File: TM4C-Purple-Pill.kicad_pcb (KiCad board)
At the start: 2 copper layers, 20.3 x 55.9 mm, 31 parts, among them IC1 TM4C123GH6PMI7R, J1 Conn_01x22, J2 Conn_01x22, J3 Conn_02x05_Odd_Even, J5 USB_B_Micro, U1 TLV75533PDBV, Y1 ABM3-16.000MHZ-B2-T, Y2 AB26TRB-32.768KHZ-T

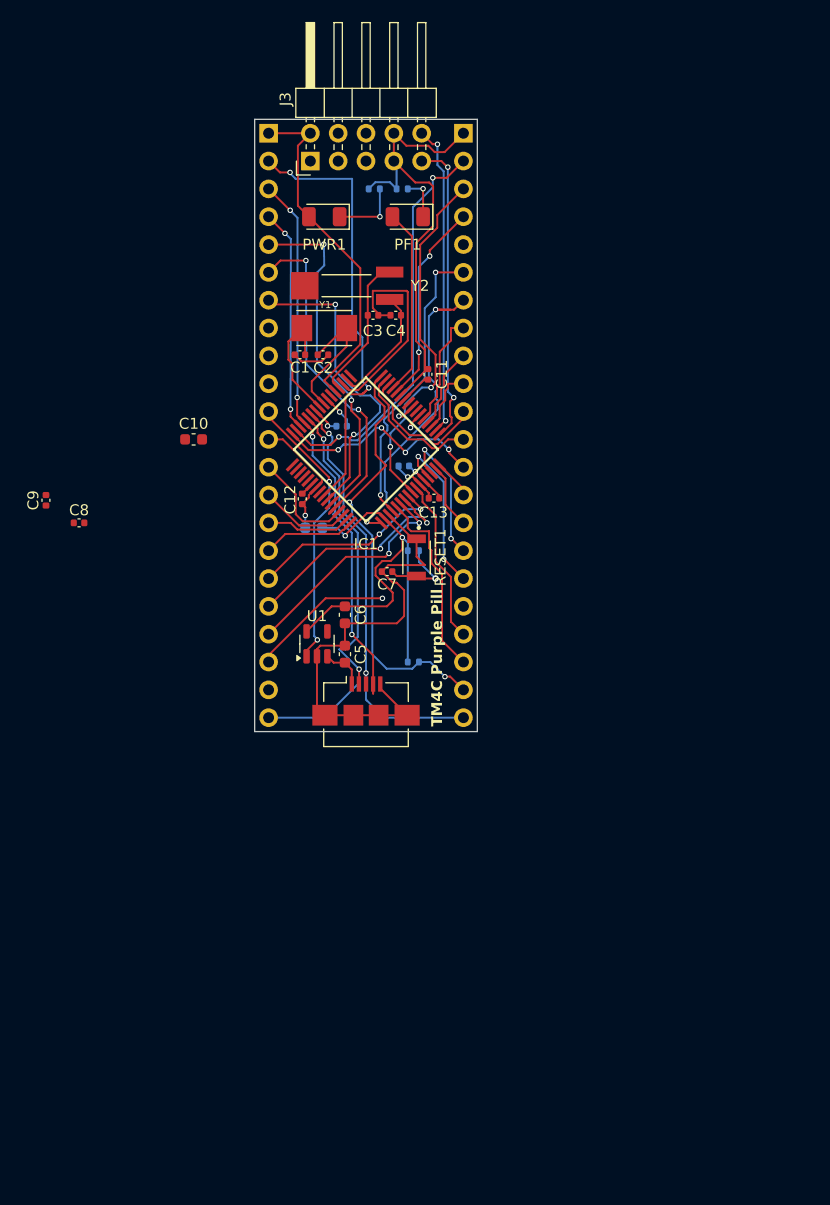
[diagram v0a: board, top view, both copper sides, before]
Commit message: Rehauled GPIO pinout. Need to find NRST wiring
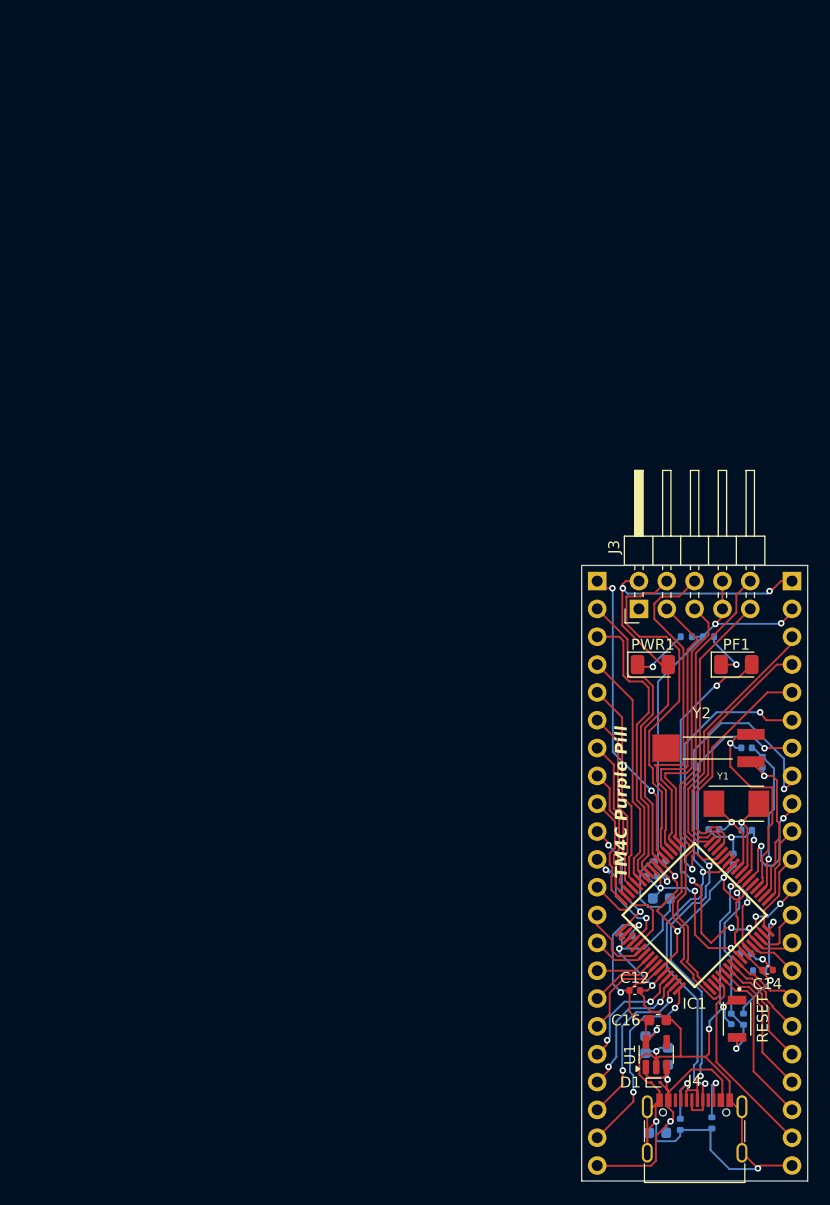
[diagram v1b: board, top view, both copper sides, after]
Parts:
- removed J5: USB_B_Micro, Connector_USB:USB_Micro-B_Amphenol_10104110_Horizontal
- removed RESET1: B3U-1000P, B3U-1000P:SW_B3U-1000P
- added 5.1k1: R5, Resistor_SMD:R_0402_1005Metric, B.Cu at (142.1, 141.1)
- added C17: 1uF, Capacitor_SMD:C_0603_1608Metric, B.Cu at (137.1, 142.0)
- added D1: ESD9B3.3ST5G, Diode_SMD:D_SOD-923, F.Cu at (136.9, 137.4)
- added J4: USB_C_Receptacle_USB2.0_16P, Connector_USB:USB_C_Receptacle_G-Switch_GT-USB-7010ASV, F.Cu at (140.5, 142.8)
- added R4: 5.1k, Resistor_SMD:R_0402_1005Metric, B.Cu at (139.2, 141.3)
- added RESET: B3U-1000P, B3U-1000P:SW_B3U-1000P, F.Cu at (144.4, 131.6)
- C1, C10, C11, C13, C2, C3, C4, C5, C6, C7, C8, C9: moved to B.Cu
- C14, C16: moved to F.Cu
- moved C8 72.4 mm to (145.1, 125.7)
- moved C9 65.1 mm to (136.6, 118.6), turned to 0 degrees
- moved C14 63.0 mm to (147.1, 127.2)
- moved C10 59.8 mm to (137.4, 120.6)
- moved C2 58.1 mm to (145.2, 114.4)
- moved C1 57.5 mm to (142.2, 114.3)
- moved Y1 57.4 mm to (144.3, 112.0)
- moved C16 54.8 mm to (137.1, 131.7), turned to 0 degrees
- moved C12 54.2 mm to (135.0, 129.0), turned to 0 degrees
- moved Y2 53.6 mm to (141.8, 106.9)
- moved C4 52.8 mm to (146.7, 108.2), turned to 90 degrees
- moved R1 52.3 mm to (144.9, 131.7), turned to -90 degrees
- moved C3 52.2 mm to (145.2, 106.9)
- moved IC1 52.0 mm to (140.5, 122.2), turned to 45 degrees
- moved C7 51.5 mm to (143.8, 131.6), turned to -90 degrees
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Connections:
- C5 pad 2: /VIN -> /VBUS
- J1 pad 1: +3.3V -> /PD6
- J1 pad 10: /PA7 -> /PB6
- J1 pad 11: /VIN -> /PB7
- J1 pad 12: GND -> /PF4
- J1 pad 13: /PD0 -> /PE3
- J1 pad 14: /PD1 -> /PE2
- J1 pad 15: /PD2 -> /PE1
- J1 pad 16: /PD3 -> /PE0
- J1 pad 17: /PE1 -> /PD7
- J1 pad 18: /PE2 -> /PC7
- J1 pad 19: /PE3 -> /PC6
- J1 pad 20: /PF1 -> /PC5
- J1 pad 21: /NHIB -> /PC4
- J1 pad 22: /PD5 -> /VBUS
- J1 pad 3: /PB0 -> /PB4
- J1 pad 4: /PB1 -> /PE4
- J1 pad 5: /PE4 -> /PE5
- J1 pad 6: /PE5 -> /PD0
- J1 pad 7: /PB4 -> /PD1
- J1 pad 8: /PA5 -> /PD2
- J1 pad 9: /PA6 -> /PD3
- J2 pad 1: GND -> +3.3V
- J2 pad 10: /PA2 -> /NHIB
- J2 pad 11: /PF2 -> /NWAKE
- J2 pad 13: /PB3 -> /PF2
- J2 pad 14: /PC4 -> /PF1
- J2 pad 15: /PC5 -> /PF0
- J2 pad 16: /PC6 -> /PA7
- J2 pad 17: /PC7 -> /PA6
- J2 pad 18: /PD6 -> /PA5
- J2 pad 19: /PD7 -> /PA4
- J2 pad 2: /PB2 -> GND
- J2 pad 20: /PF4 -> /PA3
- J2 pad 21: /NWAKE -> /PA2
- J2 pad 22: /PD4 -> GND
- J2 pad 3: /PE0 -> /PB3
- J2 pad 4: /PF0 -> /PB2
- J2 pad 5: /NRST -> /PB1
- J2 pad 6: /PB7 -> /PB0
- J2 pad 7: /PB6 -> /PD5
- J2 pad 8: /PA4 -> /PD4
- J2 pad 9: /PA3 -> /NRST
- J3 pad 1: /RST -> /NRST
- J3 pad 5: /TDP/SWO -> /TDO/SWO
- U1 pad 1: /VIN -> /VBUS
- U1 pad 3: /VIN -> /VBUS
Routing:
- net GND: track 108.4 -> 178.0 mm, vias 3 -> 15
- net /TCK/SWCLK: track 0.00 -> 33.1 mm
- net +3.3V: track 81.3 -> 114.2 mm, vias 4 -> 9
- net /VBUS: track 0.00 -> 32.3 mm, vias 0 -> 2
- net /TMS/SWDIO: track 0.00 -> 31.3 mm
- net /VIN: track 30.1 -> 0.00 mm, vias 2 -> 0
- net /PD6: track 0.00 -> 28.2 mm, vias 0 -> 2
- net /PE0: track 33.1 -> 6.41 mm, vias 2 -> 0
- net /TDI: track 0.00 -> 26.1 mm
- net /NWAKE: track 39.2 -> 13.8 mm, vias 2 -> 1
- net /TDO/SWO: track 0.00 -> 25.2 mm
- net /NRST: track 7.38 -> 31.3 mm, vias 1 -> 4
- net /PB0: track 51.2 -> 27.7 mm, vias 4 -> 2
- net /VDDC: track 0.00 -> 18.9 mm, vias 0 -> 3
- net /PD4: track 38.4 -> 57.2 mm, vias 2 -> 3
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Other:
- board size 20.3 x 55.9 mm -> 20.6 x 56.2 mm

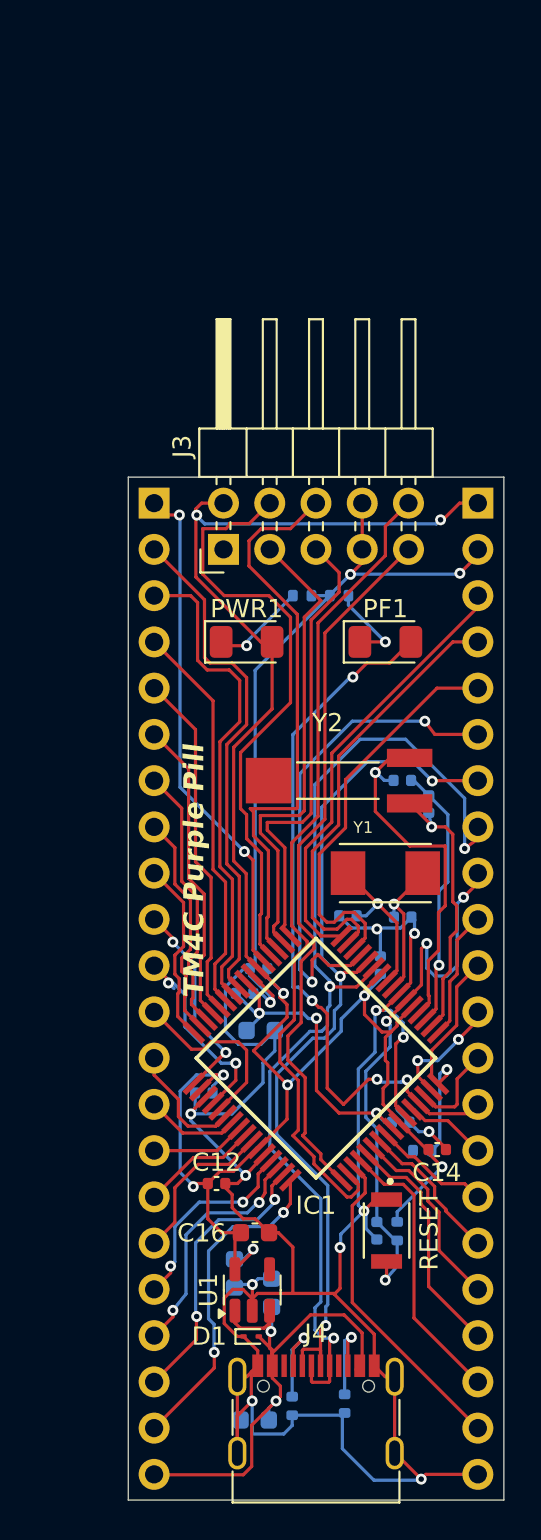
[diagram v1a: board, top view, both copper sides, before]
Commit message: Revision 0.3 with ground plane
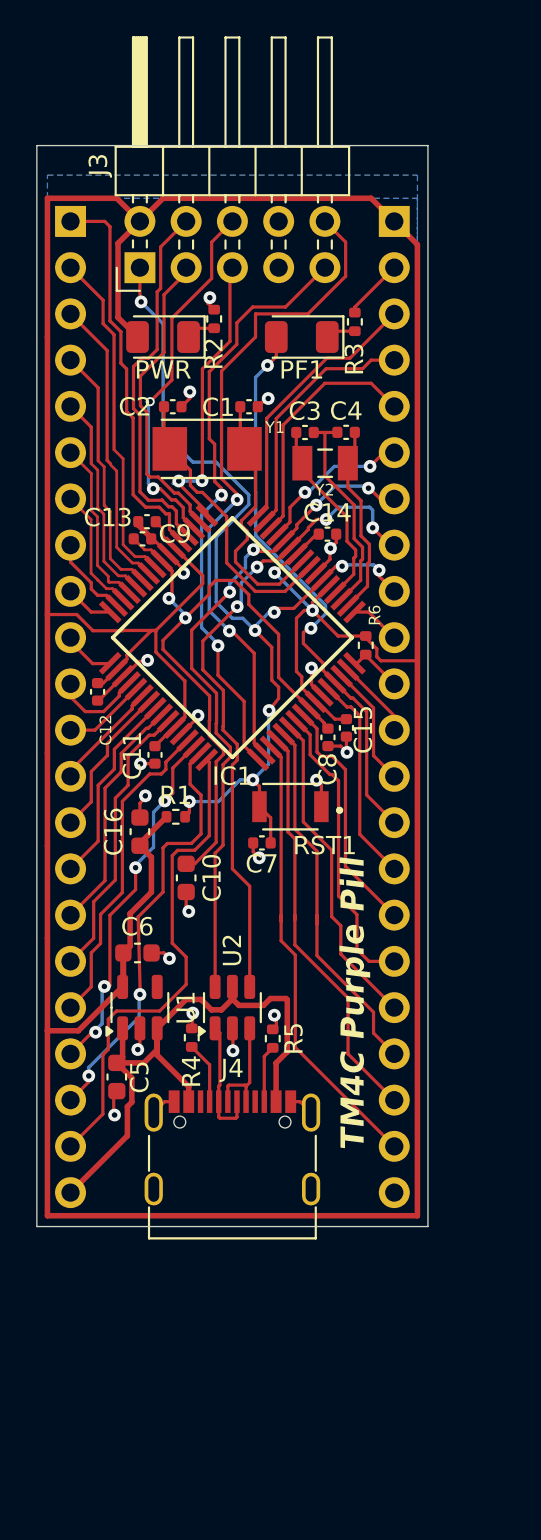
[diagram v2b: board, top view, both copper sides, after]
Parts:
- removed 5.1k1: R5, Resistor_SMD:R_0402_1005Metric
- removed C17: 1uF, Capacitor_SMD:C_0603_1608Metric
- removed D1: ESD9B3.3ST5G, Diode_SMD:D_SOD-923
- removed PWR1: LED, LED_SMD:LED_1206_3216Metric
- removed RESET: B3U-1000P, B3U-1000P:SW_B3U-1000P
- added PWR: LED, LED_SMD:LED_1206_3216Metric, F.Cu at (132.1, 82.5)
- added R5: 5.1k, Resistor_SMD:R_0402_1005Metric, F.Cu at (138.1, 121.1)
- added RST1: B3U-1000P, B3U-1000P:SW_B3U-1000P, F.Cu at (139.1, 108.3)
- added U2: USBLC6-2SC6, Package_TO_SOT_SMD:SOT-23-6, F.Cu at (135.9, 119.4)
- C1, C10, C11, C13, C15, C2, C3, C4, C5, C6, C7, C8, C9, R1, R2, R3, R4, R6: moved to F.Cu
- Y2: value AB26TRB-32.768KHZ-T -> ABS07-32.768KHZ-T; footprint AB26TRB-32.768KHZ-T:XTAL_AB26TRB-32.768KHZ-T -> ABS07-32.768KHZ-T:XTAL_ABS07-32.768KHZ-T
- moved C14 34.3 mm to (141.1, 93.4)
- moved C13 31.5 mm to (131.2, 92.7)
- moved C2 30.7 mm to (132.6, 86.4)
- moved C1 28.5 mm to (136.8, 86.4), turned to 0 degrees
- moved R6 27.9 mm to (143.2, 99.5), turned to -90 degrees
- moved C12 27.8 mm to (128.5, 102.0), turned to -90 degrees
- moved R1 25.8 mm to (132.8, 108.9), turned to 0 degrees
- moved C9 25.6 mm to (131.0, 93.6)
- moved Y1 25.3 mm to (134.5, 88.7), turned to 180 degrees
- moved IC1 23.5 mm to (135.9, 99.1)
- moved C16 22.9 mm to (130.8, 109.7), turned to 90 degrees
- moved C7 22.2 mm to (137.5, 110.3), turned to 180 degrees
- moved C8 21.5 mm to (141.1, 104.5), turned to -90 degrees
- moved R4 21.0 mm to (133.7, 121.0), turned to 90 degrees
- moved C4 20.9 mm to (142.1, 87.8), turned to 180 degrees
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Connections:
- J4 pad A6: /PD4 -> Net-(J4-D+-PadA6)
- J4 pad A7: /PD5 -> Net-(J4-D--PadA7)
- J4 pad B6: /PD4 -> Net-(J4-D+-PadA6)
- J4 pad B7: /PD5 -> Net-(J4-D--PadA7)
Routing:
- net GND: track 178.0 -> 40.3 mm, vias 15 -> 20
- net +3.3V: track 114.2 -> 227.4 mm, vias 9 -> 2
- net /NRST: track 31.3 -> 55.0 mm, vias 4 -> 8
- net /PD4: track 57.2 -> 36.3 mm, vias 3 -> 4
- net /PB0: track 27.7 -> 9.29 mm
- net /VDDC: track 18.9 -> 36.6 mm, vias 3 -> 2
- net /PD5: track 49.3 -> 36.5 mm, vias 3 -> 4
- net /TCK/SWCLK: track 33.1 -> 20.4 mm
- net /TMS/SWDIO: track 31.3 -> 20.3 mm, vias 0 -> 2
- net /NWAKE: track 13.8 -> 3.07 mm, vias 1 -> 0
- net /PB4: track 26.9 -> 16.2 mm
- net /PB2: track 24.0 -> 13.8 mm
- net /XOSC1: track 20.1 -> 10.6 mm, vias 1 -> 0
- net /PB5: track 28.1 -> 18.7 mm
- net /PB6: track 12.2 -> 2.90 mm, vias 2 -> 0
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- added copper zone on B.Cu, net GND
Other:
- board size 20.6 x 56.2 mm -> 21.5 x 59.4 mm
- rule pad_to_mask_clearance: 0 -> 0.08
